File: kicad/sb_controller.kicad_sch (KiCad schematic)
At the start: 10 parts

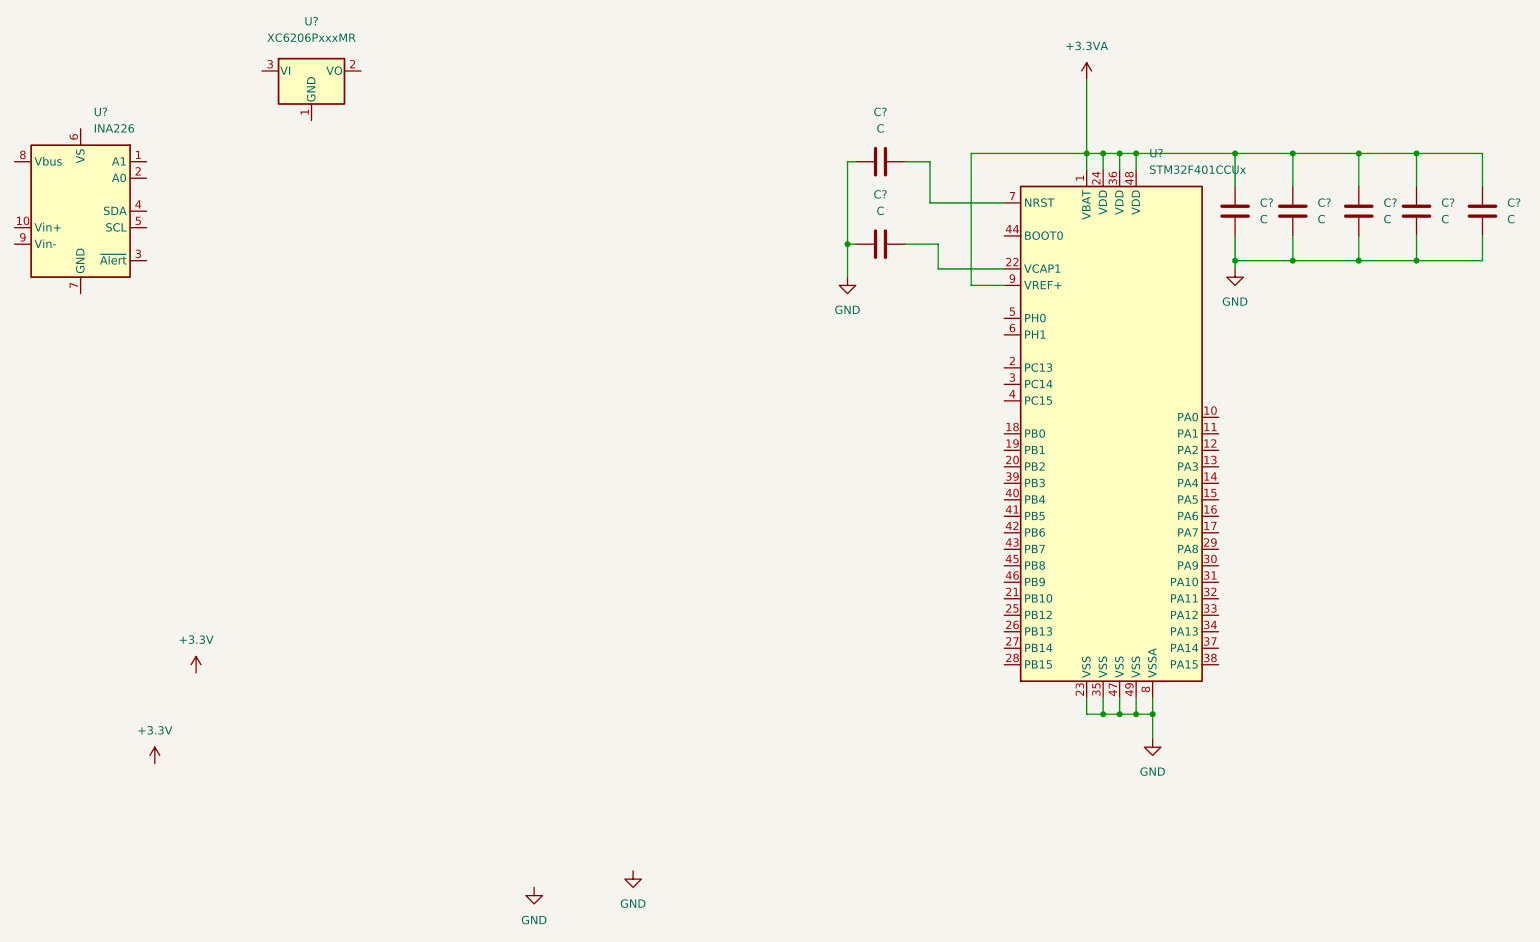
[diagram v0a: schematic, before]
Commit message: Update modules wiring
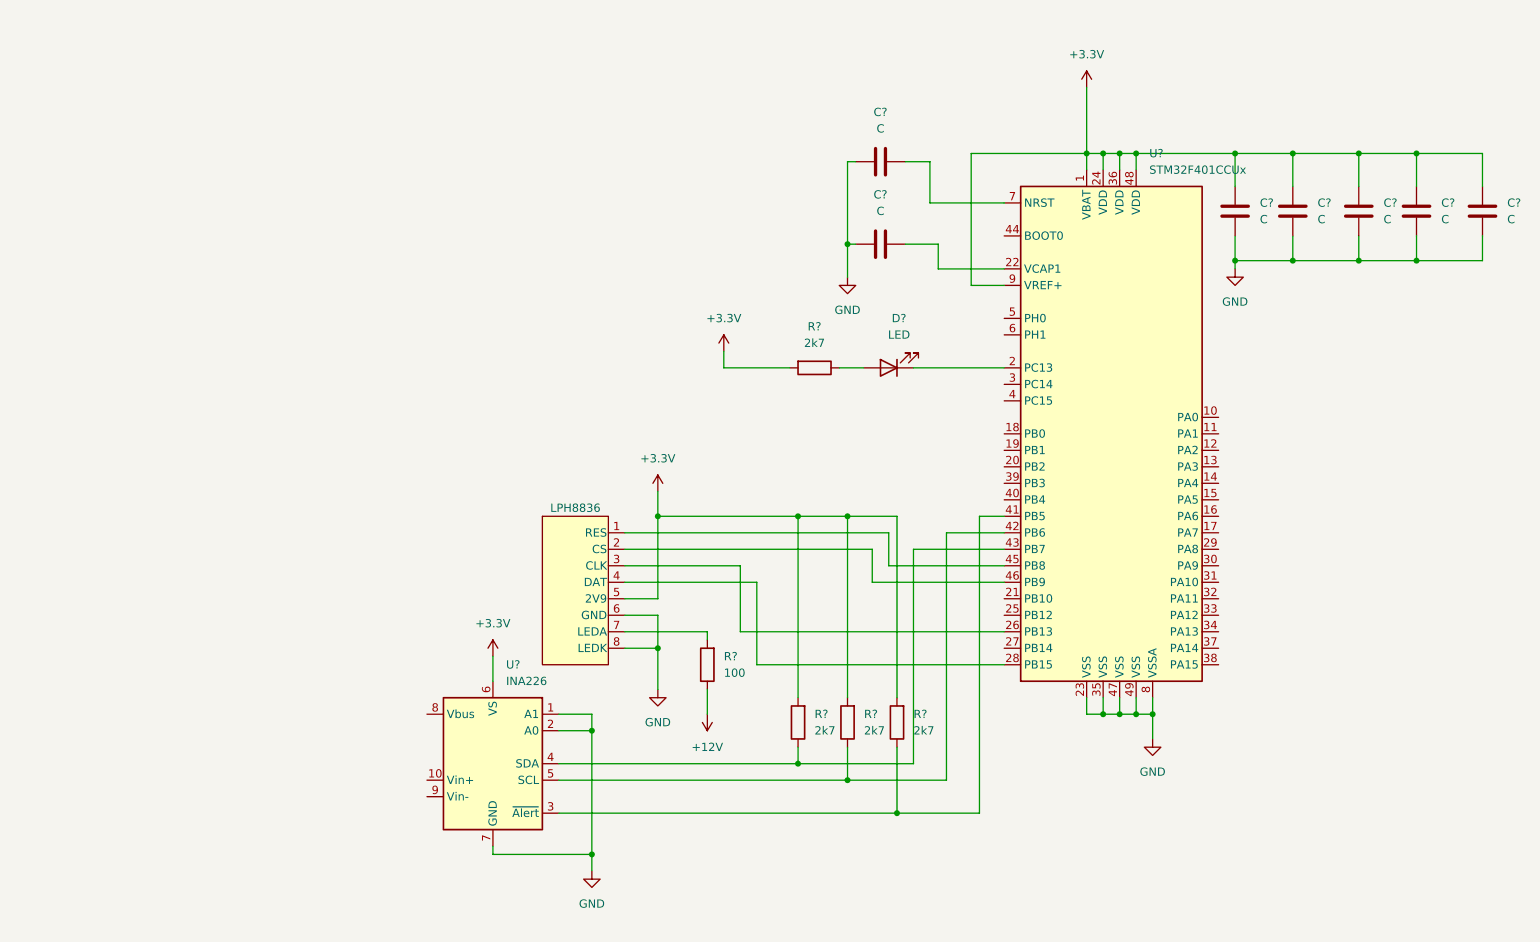
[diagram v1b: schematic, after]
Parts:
- removed U?: XC6206PxxxMR, Package_TO_SOT_SMD:SOT-23, symbol Regulator_Linear:XC6206PxxxMR
- added D?: LED, symbol Device:LED
- added R?: 100, symbol Device:R
- added R? (x4): 2k7, symbol Device:R
- added U?: LPH8836, symbol custom_symbols:LPH8836
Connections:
- net +3.3VA is gone; now on net +3.3V: C?.1, C?.1, C?.1, C?.1, C?.1, U?.1 (VBAT), U?.24 (VDD), U?.36 (VDD), U?.48 (VDD), U?.9 (VREF+)
- net +3.3V: now also U?.6 (VS), R?.2, R?.2, R?.2, R?.2, U?.5 (2V9)
- net GND: now also U?.1 (A1), U?.2 (A0), U?.7 (GND), U?.6 (GND), U?.8 (LEDK)
- net at U?.3 (~{Alert}): now also U?.41 (PB5), R?.1
- net at U?.4 (SDA): now also U?.43 (PB7), R?.1
- net at U?.5 (SCL): now also U?.42 (PB6), R?.1
- net at U?.2 (PC13): now also D?.1 (K)
- net at U?.26 (PB13): now also U?.3 (CLK)
- net at U?.28 (PB15): now also U?.4 (DAT)
- net at U?.45 (PB8): now also U?.1 (RES)
- net at U?.46 (PB9): now also U?.2 (CS)
- new net: R?.2, U?.7 (LEDA)
- new net: D?.2 (A), R?.1
- new net +12V: R?.1
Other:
- moved on the sheet: U?
